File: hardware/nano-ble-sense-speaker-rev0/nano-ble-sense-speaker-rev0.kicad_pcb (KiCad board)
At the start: 2 copper layers, 1 part, among them J1 Arduino-NANO-33

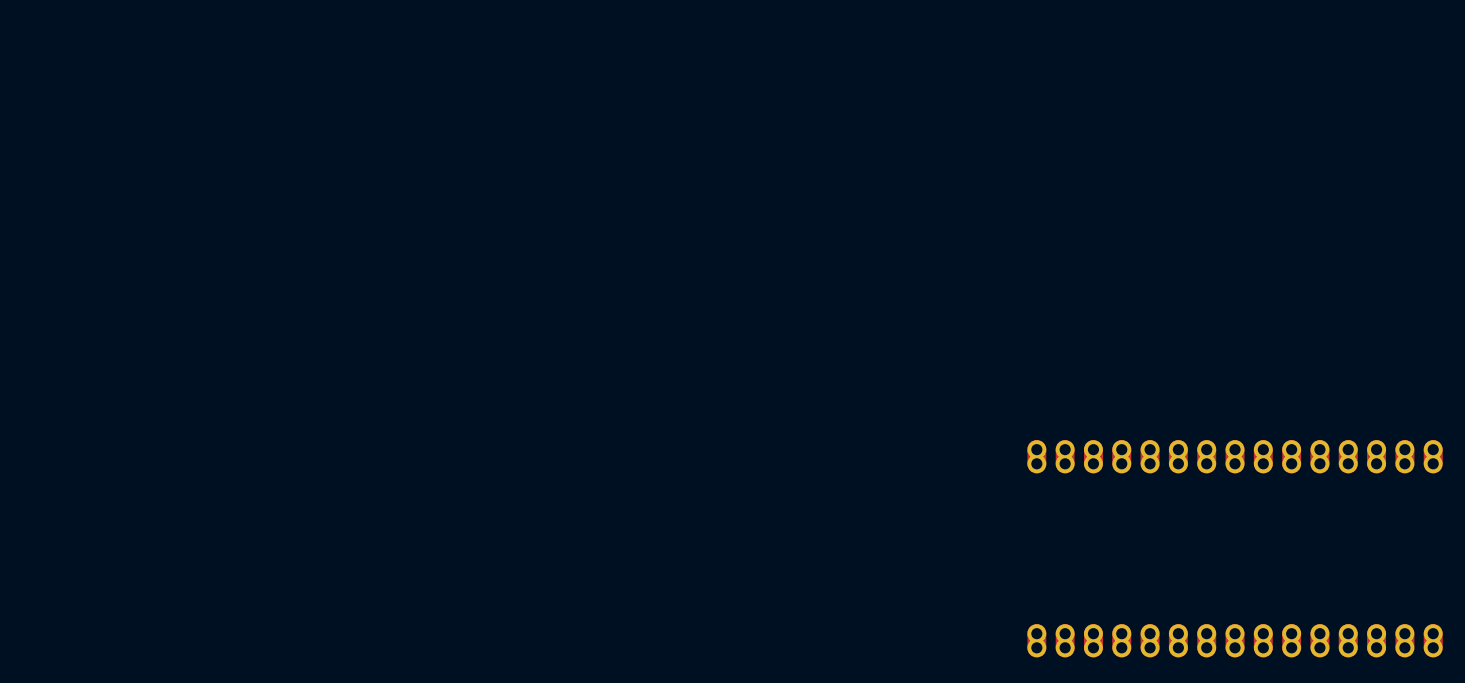
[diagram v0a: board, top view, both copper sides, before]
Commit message: Make first PCB design
PCB Design in KiCAD now has:
- OLED 1.3inch
- power supply using LM7805 and capacitors

TODO:
- Add I2S module either as the breakout board of on the PCB as an SMD
comp.
- Move components a little more closer.
- Add PCB ground pad, and make paths between all components.
- Add pull up resistors to the OLED I2C pins

Signed-off-by: Dhruva Gole <goledhruva@gmail.com>
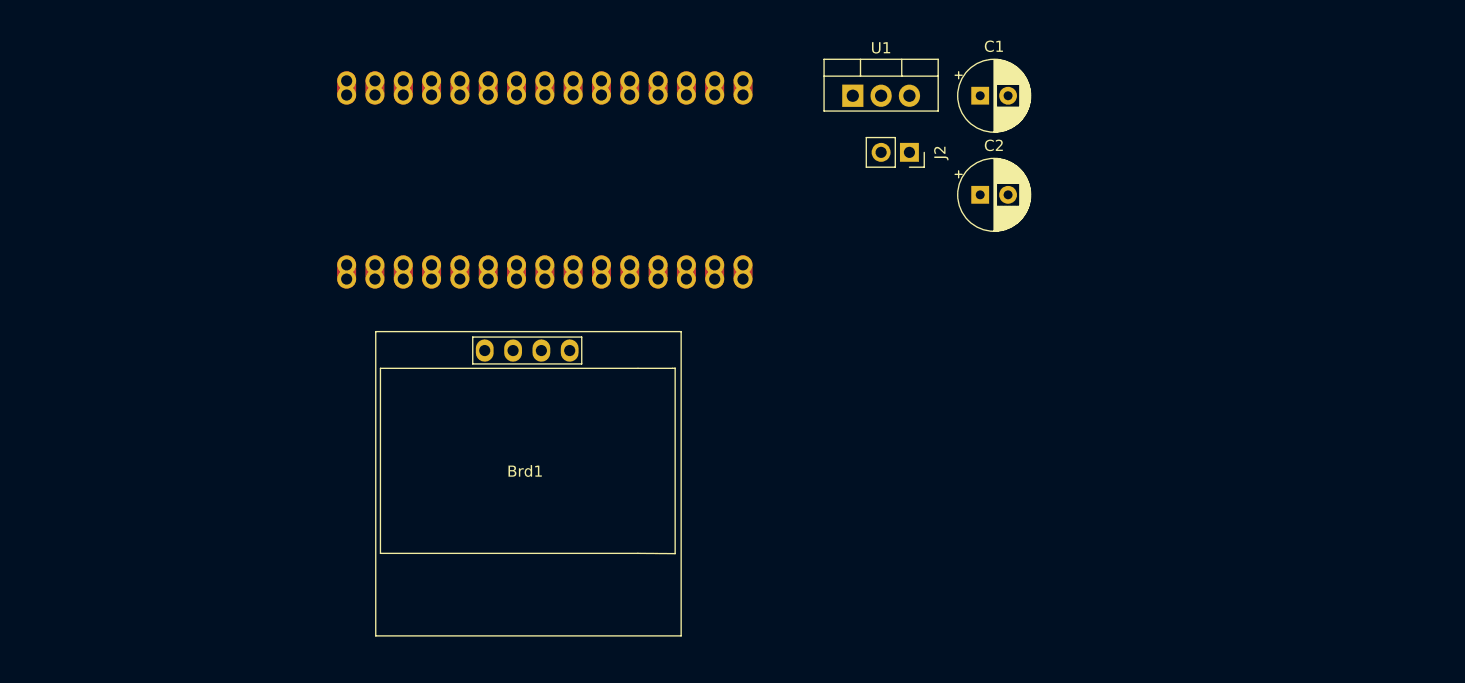
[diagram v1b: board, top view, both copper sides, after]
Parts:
- added Brd1: SSD1306, SSD1306:128x64OLED, F.Cu at (83.6, 98.2)
- added C1: C, Capacitor_THT:CP_Radial_D6.3mm_P2.50mm, F.Cu at (124.5, 64.8)
- added C2: C, Capacitor_THT:CP_Radial_D6.3mm_P2.50mm, F.Cu at (124.5, 73.7)
- added J2: Conn_01x02_Female, Connector_PinSocket_2.54mm:PinSocket_1x02_P2.54mm_Vertical, F.Cu at (118.1, 69.8)
- added U1: LM78L05_TO92, Package_TO_SOT_THT:TO-220-3_Vertical, F.Cu at (113.0, 64.8)
- moved J1 70.2 mm to (85.4, 72.3)
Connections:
- J1 pad 14: Net-(J1-Pad14) -> GND
- J1 pad 15: Net-(J1-Pad15) -> 5V
- J1 pad 2: Net-(J1-Pad2) -> 3V3
- J1 pad 8: Net-(J1-Pad8) -> OLED_SDA
- J1 pad 9: Net-(J1-Pad9) -> OLED_SCL
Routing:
- net Net-(J1-Pad30): track 0.64 -> 0.00 mm

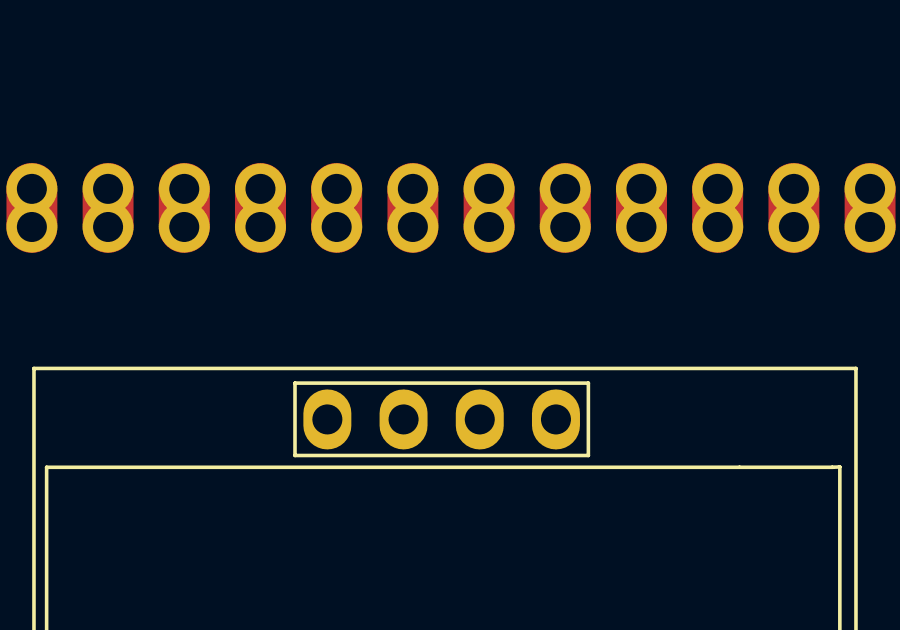
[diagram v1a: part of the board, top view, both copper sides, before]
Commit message: Add pull up resistors to I2C
Signed-off-by: Dhruva Gole <goledhruva@gmail.com>
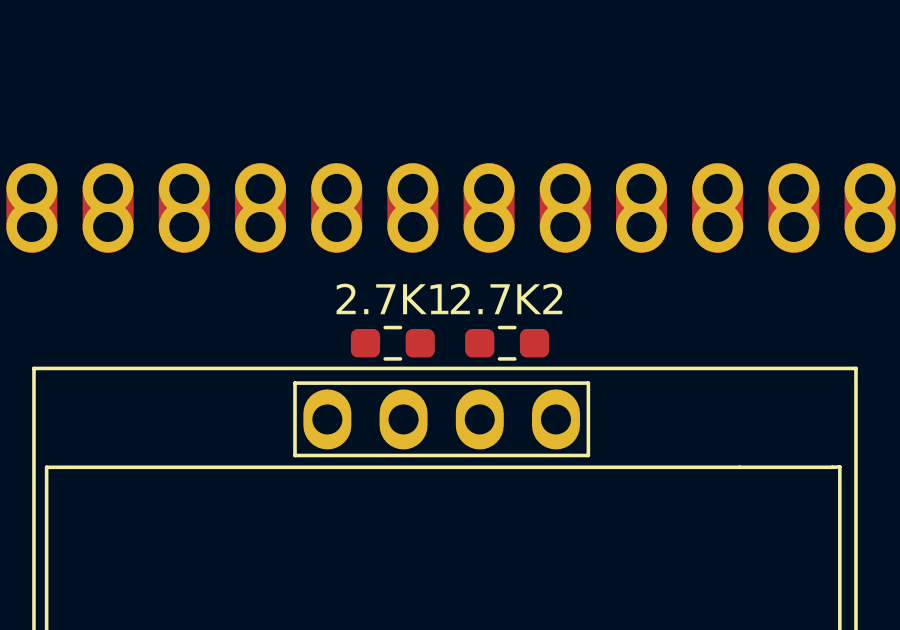
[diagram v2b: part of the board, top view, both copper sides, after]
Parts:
- added 2.7K1: R, Resistor_SMD:R_0603_1608Metric_Pad0.98x0.95mm_HandSolder, F.Cu at (82.2, 85.1)
- added 2.7K2: R, Resistor_SMD:R_0603_1608Metric_Pad0.98x0.95mm_HandSolder, F.Cu at (86.0, 85.1)

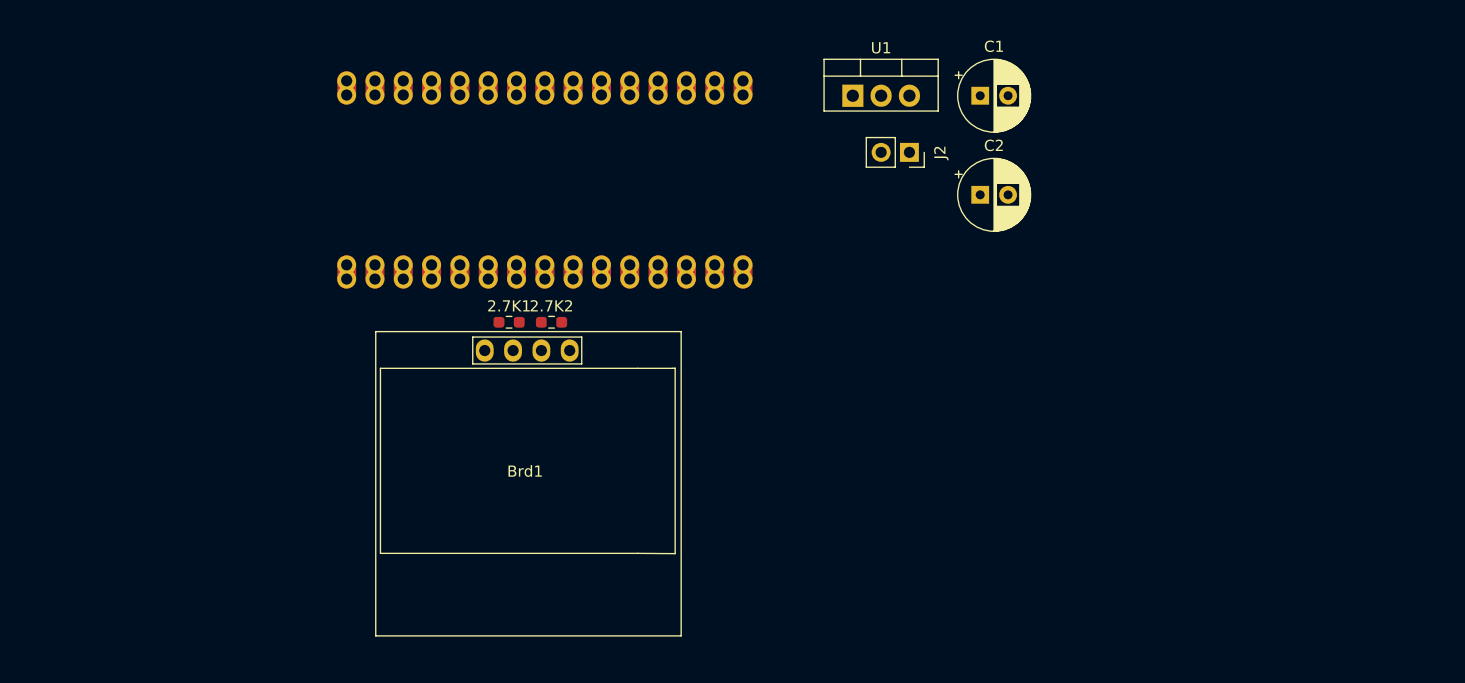
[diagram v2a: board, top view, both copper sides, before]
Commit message: Update PCB design
- Now includes bar LED with all it's connections
- 3D files for OLED and arduino

TODO:
- Draw traces
- Make drill holes for mounting the OLED steadily
- Probably add a Li ion charging circuit

Signed-off-by: Dhruva Gole <goledhruva@gmail.com>
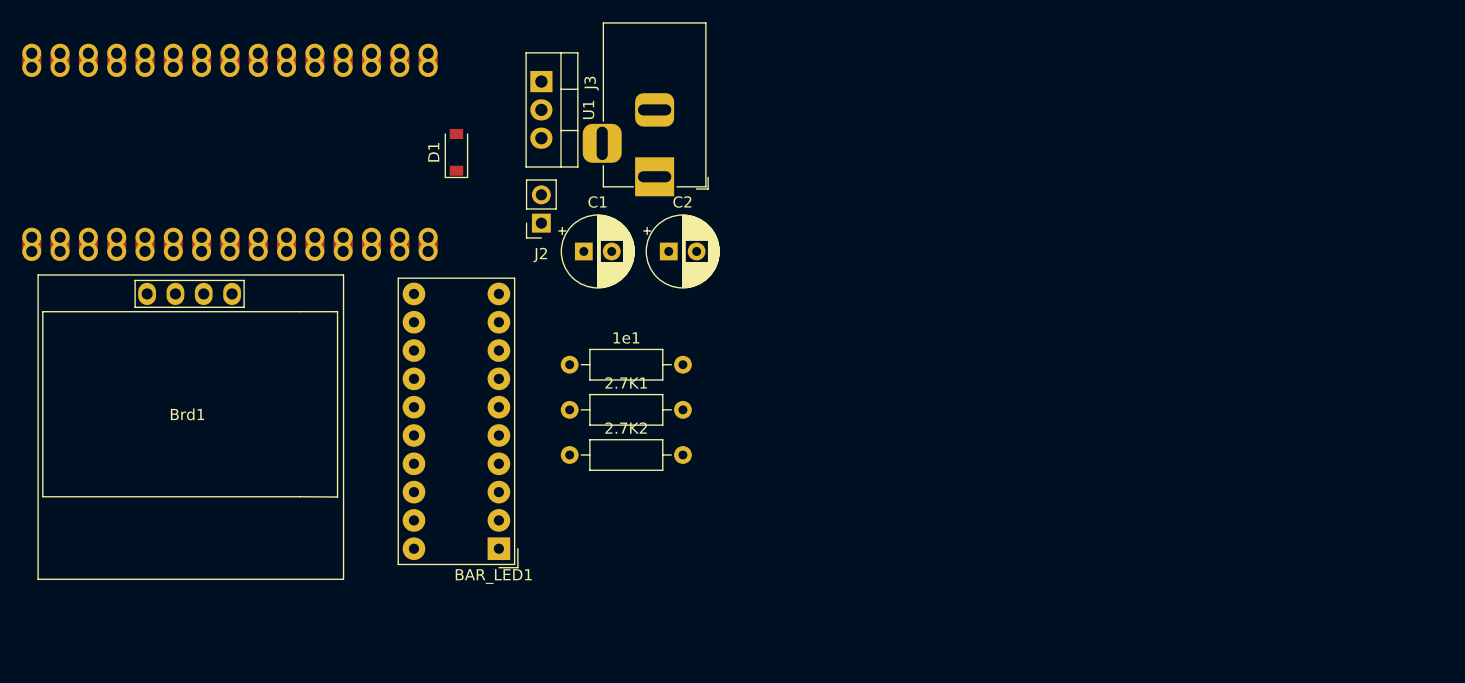
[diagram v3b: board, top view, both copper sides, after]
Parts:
- added 1e1: R, Resistor_THT:R_Axial_DIN0207_L6.3mm_D2.5mm_P10.16mm_Horizontal, F.Cu at (87.6, 88.9)
- added BAR_LED1: HDSP-4830_2, Display:HDSP-4830, F.Cu at (81.3, 105.4)
- added D1: D_Schottky, Diode_SMD:D_SOD-123, F.Cu at (77.5, 69.8)
- added J3: Barrel_Jack, Connector_BarrelJack:BarrelJack_Horizontal, F.Cu at (95.2, 72.0)
- 2.7K1, 2.7K2: footprint Resistor_SMD:R_0603_1608Metric_Pad0.98x0.95mm_HandSolder -> Resistor_THT:R_Axial_DIN0207_L6.3mm_D2.5mm_P10.16mm_Horizontal
- moved C1 38.2 mm to (88.9, 78.7)
- moved J2 33.6 mm to (85.1, 76.2), turned to 180 degrees
- moved Brd1 30.7 mm to (53.3, 93.2)
- moved C2 28.4 mm to (96.5, 78.7)
- moved J1 28.4 mm to (57.1, 69.8)
- moved U1 28.0 mm to (85.1, 63.5), turned to 270 degrees
- moved 2.7K2 12.0 mm to (87.6, 97.0)
- moved 2.7K1 9.56 mm to (87.6, 93.0)
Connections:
- C1 pad 1: +9V -> Net-(C1-Pad1)
- J1 pad 20: Net-(J1-Pad20) -> BAR_LED1
- J1 pad 21: Net-(J1-Pad21) -> BAR_LED2
- J1 pad 22: Net-(J1-Pad22) -> BAR_LED3
- J1 pad 23: Net-(J1-Pad23) -> BAR_LED4
- J1 pad 24: Net-(J1-Pad24) -> BAR_LED5
- J1 pad 25: Net-(J1-Pad25) -> BAR_LED6
- J1 pad 26: Net-(J1-Pad26) -> BAR_LED7
- J1 pad 27: Net-(J1-Pad27) -> BAR_LED8
- J1 pad 28: Net-(J1-Pad28) -> BAR_LED9
- J1 pad 29: Net-(J1-Pad29) -> BAR_LED10
- U1 pad 3: +9V -> Net-(C1-Pad1)

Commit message: Minor changes
Signed-off-by: Dhruva Gole <goledhruva@gmail.com>
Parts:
- added MQ_Conn1: Conn_01x04_Male, MQ-sensor:MQ-3, F.Cu at (97.8, 86.4)
